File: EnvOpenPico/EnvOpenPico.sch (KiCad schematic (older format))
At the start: 47 parts, among them J2 SKRKAEE020, J3 2.54mm header 01x20, J4 2.54mm header 01x20, J5 Conn_01x03_Male, U1 TPS63002, U3 RP2040, X1 XO 32 12Mhz 3225 seiko

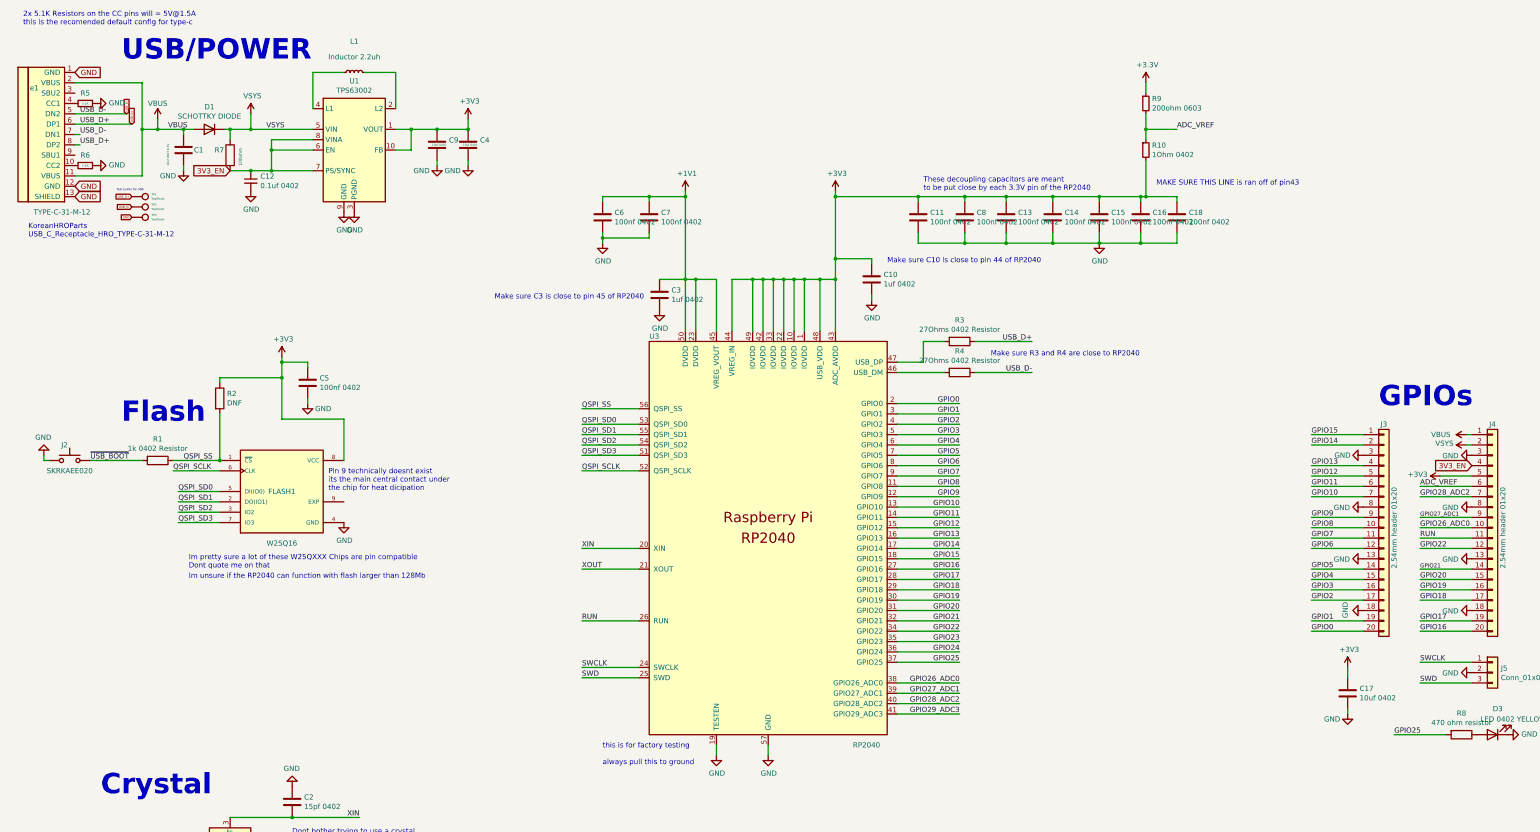
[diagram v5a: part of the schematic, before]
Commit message: added some extra notes and moved some parts about, added some test points.
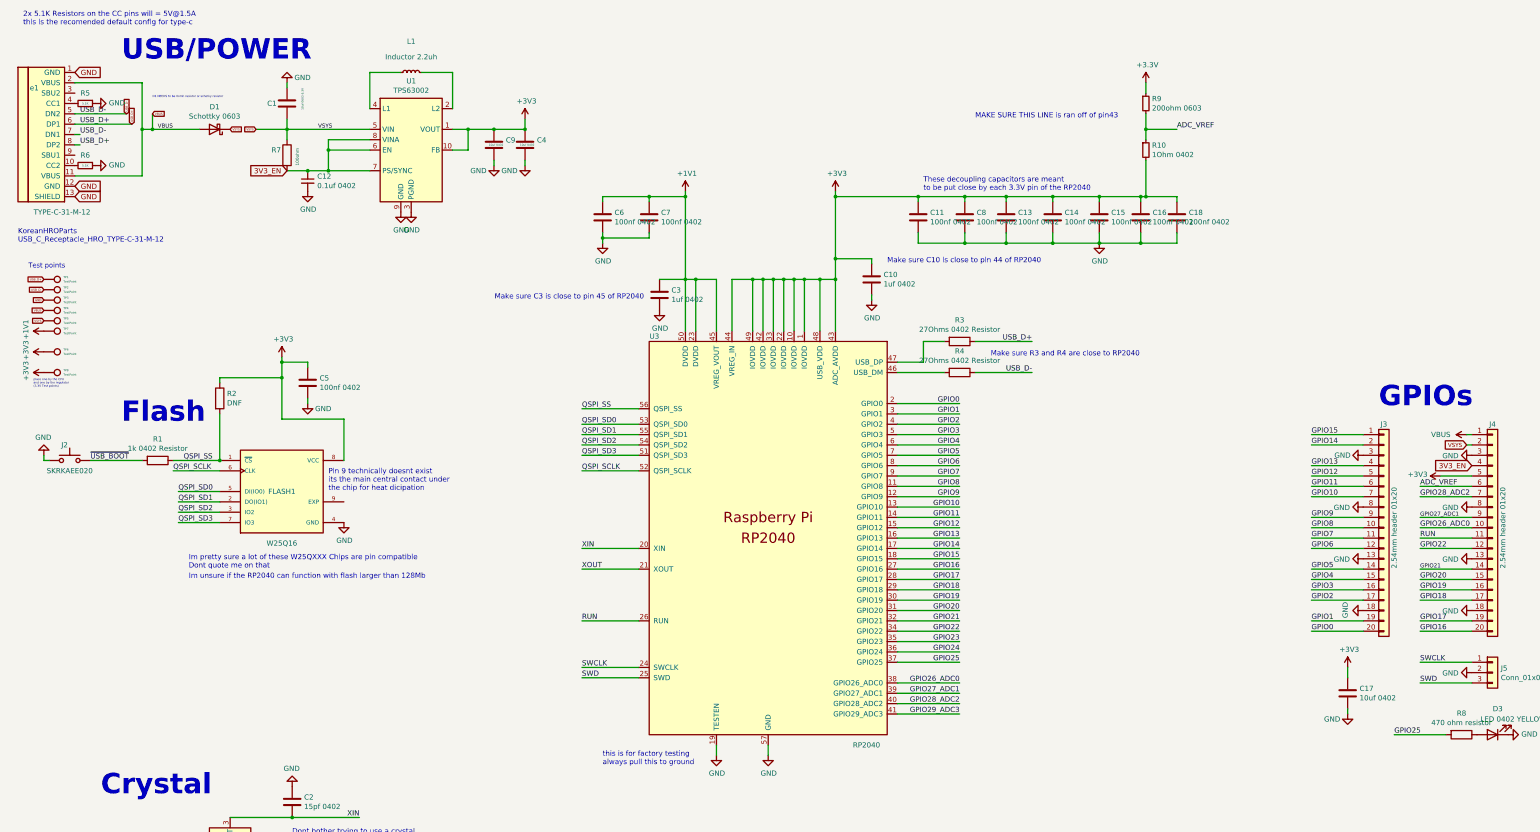
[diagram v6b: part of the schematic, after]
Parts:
- removed D1: SCHOTTKY DIODE, Diode_SMD:D_0603_1608Metric, symbol Simulation_SPICE:DIODE
- added D1: Schottky 0603, Diode_SMD:D_0603_1608Metric, symbol Device:D_Schottky
- added TP4, TP5, TP6, TP7, TP8: TestPoint, TestPoint:TestPoint_Pad_D1.0mm, symbol Connector:TestPoint
- TP1, TP2, TP3: footprint TestPoint:TestPoint_Pad_1.0x1.0mm -> TestPoint:TestPoint_Pad_D1.0mm
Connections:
- net +1V1: now also TP7.1
- net +3V3: now also TP6.1, TP8.1
- net VBUS: now also D1.2 (A), TP4.1; no longer C1.1, J4.2 (Pin_2), R7.1, U1.5 (VIN)
- new net VSYS: C1.1, D1.1 (K), J4.2 (Pin_2), R7.1, TP5.1, U1.5 (VIN)
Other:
- note added: "D1 NEEDS to be 0omh resistor or schotky resistor"
- note added: "Test points"
- note added: "place one by the CPU\nand one by the regulator\n(3.3V Test points)"
- note added: "this is for factory testing\nalways pull this to ground"
- note removed: "Test points for USB"
- note removed: "this is for factory testing\n\nalways pull this to ground"
- moved on the sheet: C1, C12, C4, C9, L1, R7, TP1, TP2, TP3, U1

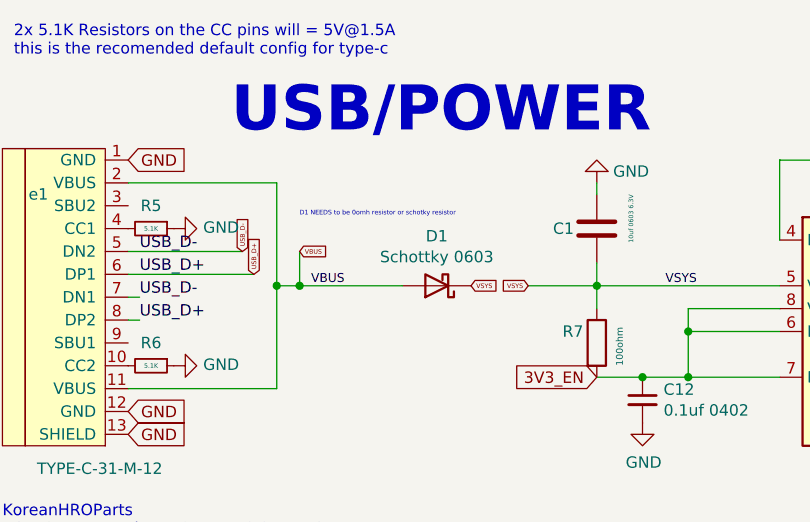
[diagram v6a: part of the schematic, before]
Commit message: changed notes regarding D1 and what type should be installed.
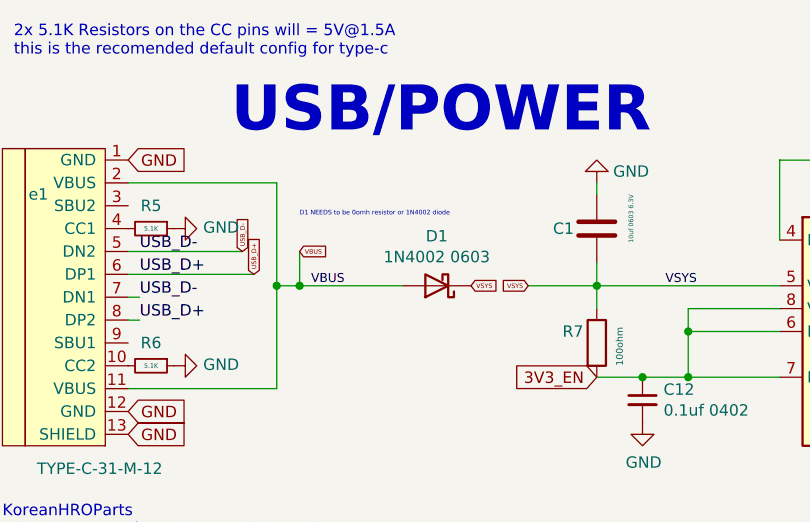
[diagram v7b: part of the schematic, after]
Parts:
- D1: value Schottky 0603 -> 1N4002 0603
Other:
- note added: "D1 NEEDS to be 0omh resistor or 1N4002 diode"
- note removed: "D1 NEEDS to be 0omh resistor or schotky resistor"
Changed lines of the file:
@@
 P 2450 1750
 F 0 "D1" H 2450 1533 50  0000 C CNN
-F 1 "Schottky 0603" H 2450 1624 50  0000 C CNN
+F 1 "1N4002 0603" H 2450 1624 50  0000 C CNN
 F 2 "Diode_SMD:D_0603_1608Metric" H 2450 1750 50  0001 C CNN
 F 3 "~" H 2450 1750 50  0001 C CNN
@@
 $EndComp
 Text Notes 1850 1450 0    20   ~ 0
-D1 NEEDS to be 0omh resistor or schotky resistor
+D1 NEEDS to be 0omh resistor or 1N4002 diode
 Wire Wire Line
 	3950 1200 4250 1200

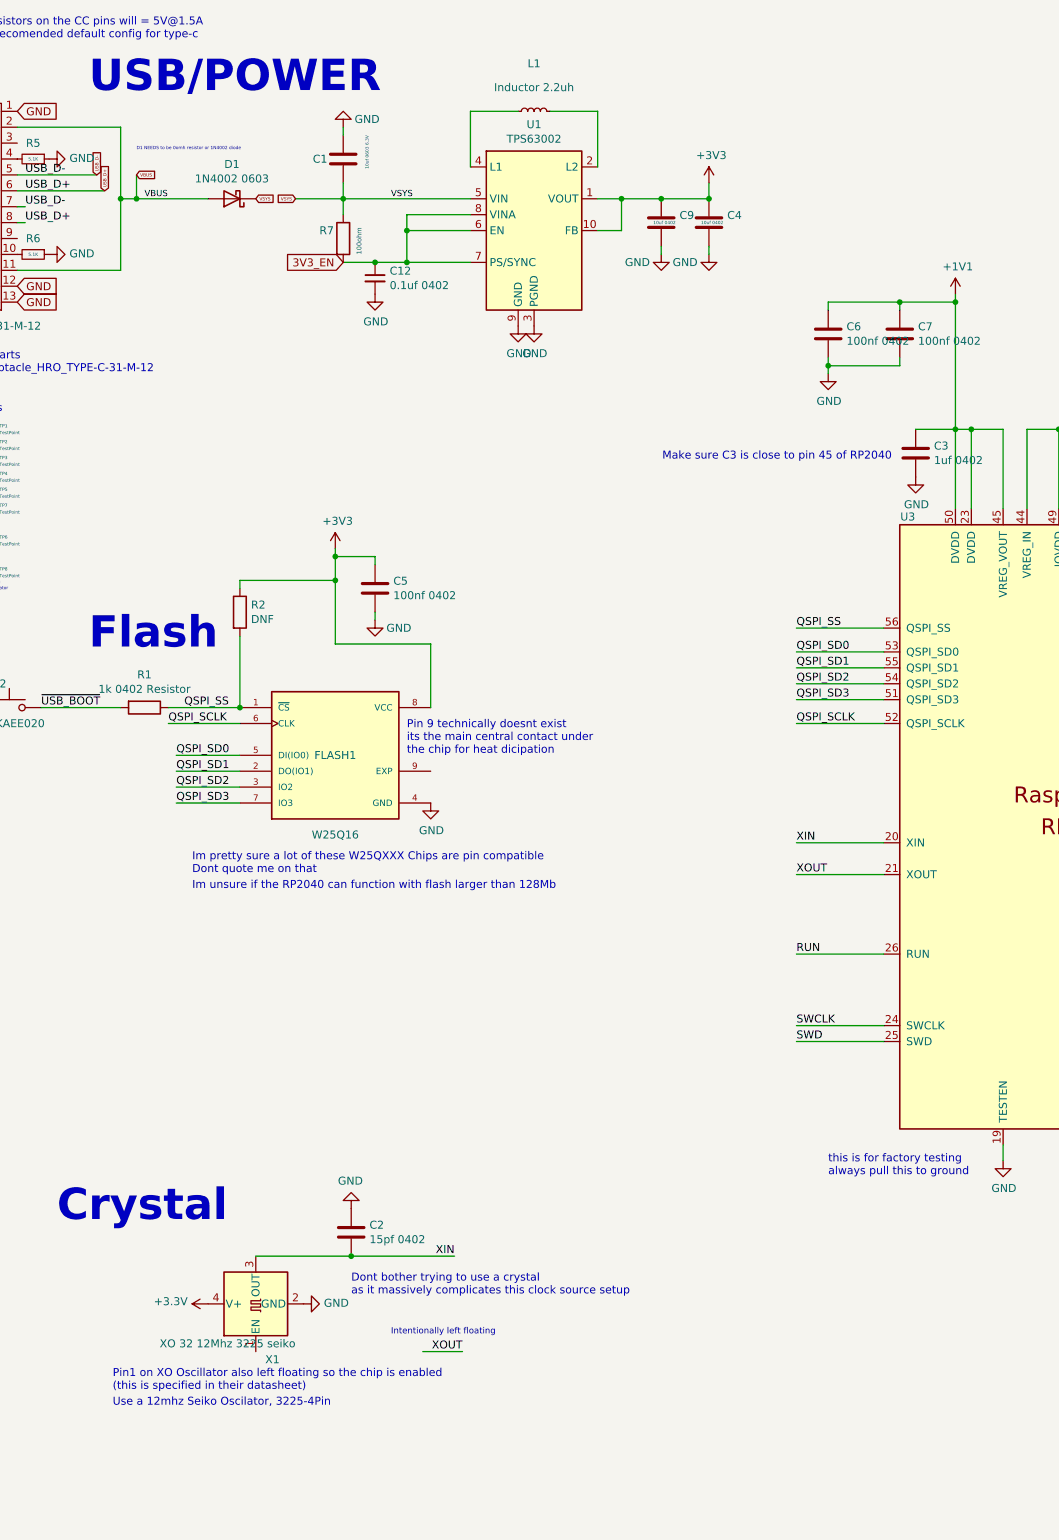
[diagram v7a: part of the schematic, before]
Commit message: replaced XO with crystal due to stock issues, and some general cleanups and corrections
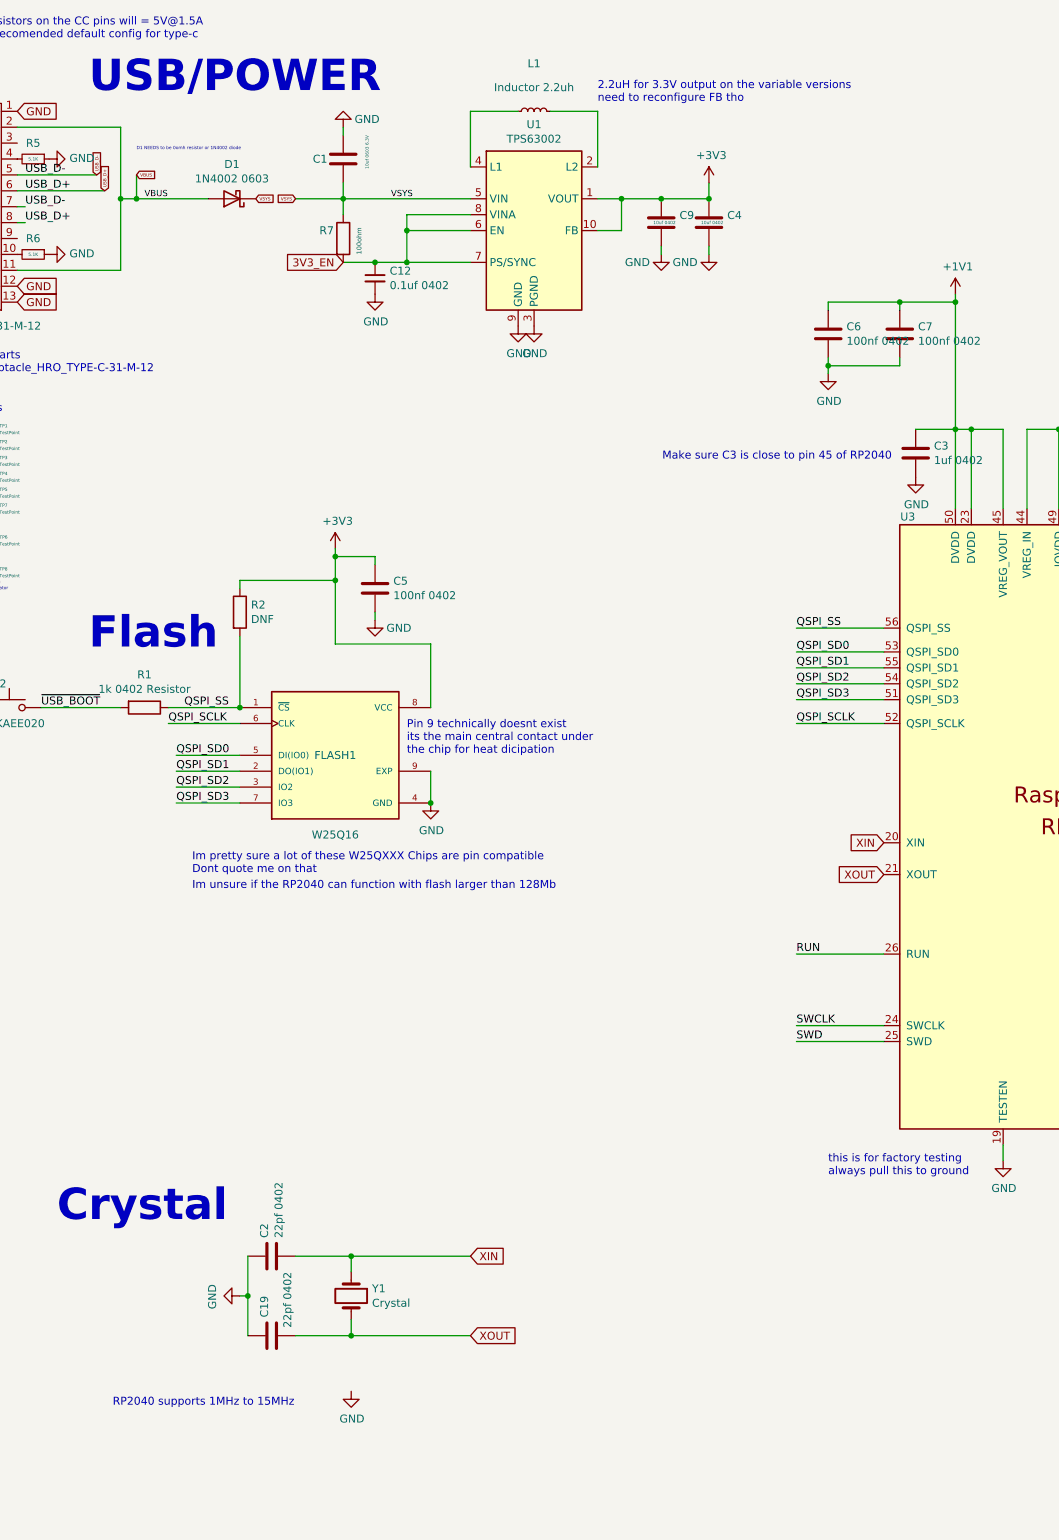
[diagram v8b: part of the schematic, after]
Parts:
- removed X1: XO 32 12Mhz 3225 seiko, Crystal:Crystal_SMD_SeikoEpson_TSX3225-4Pin_3.2x2.5mm, symbol Oscillator:XO32
- added C19: 22pf 0402, Capacitor_SMD:C_0402_1005Metric, symbol Device:C
- added Y1: Crystal, Crystal:Crystal_SMD_5032-2Pin_5.0x3.2mm, symbol Device:Crystal
- C2: value 15pf 0402 -> 22pf 0402
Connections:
- net GND: now also FLASH1.9 (EXP), C19.1
- net XIN: now also Y1.1
- net XOUT: now also C19.2, Y1.2
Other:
- note added: "2.2uH for 3.3V output on the variable versions\nneed to reconfigure FB tho"
- note added: "RP2040 supports 1MHz to 15MHz"
- note removed: "Dont bother trying to use a crystal\nas it massively complicates this clock source setup"
- note removed: "Intentionally left floating"
- note removed: "Pin1 on XO Oscillator also left floating so the chip is enabled\n(this is specified in their datasheet)"
- note removed: "Use a 12mhz Seiko Oscilator, 3225-4Pin"
- moved on the sheet: C2
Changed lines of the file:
@@
 encoding utf-8
 Sheet 1 1
-Title "RP2040 Minimal Design Example"
+Title "Raspberry Pi Pico Clone"
 Date "2020-12-18"
 Rev "REV1"
-Comp "Raspberry Pi (Trading) Ltd"
+Comp "Envious.Design"
 Comment1 ""
 Comment2 ""
@@
 	1    0    0    -1
 $EndComp
-Wire Wire Line
-	6000 5800 6550 5800
-Wire Wire Line
-	6550 6000 6000 6000
 Wire Wire Line
 	6000 4600 6550 4600
@@
 Text Label 6000 4900 0    50   ~ 0
 QSPI_SD3
-Text Label 6000 5800 0    50   ~ 0
-XIN
-Text Label 6000 6000 0    50   ~ 0
-XOUT
 $Comp
 L Device:R R4
@@
 Wire Wire Line
 	13400 6950 13400 7050
-Text Label 3850 8400 2    50   ~ 0
-XIN
-Text Label 3900 9000 2    50   ~ 0
-XOUT
-Wire Wire Line
-	2600 8400 3200 8400
 Text Notes 9950 3950 0    50   ~ 0
 Make sure R3 and R4 are close to RP2040
@@
 	8450 2400 9250 2400
 $Comp
-L Oscillator:XO32 X1
-U 1 1 60894744
-P 2600 8700
-F 0 "X1" V 2250 8550 50  0000 L CNN
-F 1 "XO 32 12Mhz 3225 seiko" V 2350 8450 50  0000 L CNN
-F 2 "Crystal:Crystal_SMD_SeikoEpson_TSX3225-4Pin_3.2x2.5mm" H 3300 8350 50  0001 C CNN
-F 3 "" H 2500 8700 50  0001 C CNN
-	1    2600 8700
-	0    -1   -1   0
-$EndComp
-$Comp
-L power:GND #PWR0105
-U 1 1 608B9527
-P 2900 8700
-F 0 "#PWR0105" H 2900 8450 50  0001 C CNN
-F 1 "GND" V 2905 8572 50  0000 R CNN
-F 2 "" H 2900 8700 50  0001 C CNN
-F 3 "" H 2900 8700 50  0001 C CNN
-	1    2900 8700
-	0    -1   -1   0
-$EndComp
-$Comp
-L power:+3.3V #PWR0106
-U 1 1 608B9D1F
-P 2300 8700
-F 0 "#PWR0106" H 2300 8550 50  0001 C CNN
-F 1 "+3.3V" V 2315 8828 50  0000 L CNN
-F 2 "" H 2300 8700 50  0001 C CNN
-F 3 "" H 2300 8700 50  0001 C CNN
-	1    2300 8700
-	0    -1   -1   0
-$EndComp
-$Comp
 L Device:C C2
 U 1 1 5ED96B87
-P 3200 8250
-F 0 "C2" H 3315 8296 50  0000 L CNN
-F 1 "15pf 0402" H 3315 8205 50  0000 L CNN
-F 2 "Capacitor_SMD:C_0402_1005Metric" H 3238 8100 50  0001 C CNN
-F 3 "" H 3200 8250 50  0001 C CNN
-	1    3200 8250
-	1    0    0    -1
+P 2700 8400
+F 0 "C2" H 2815 8446 50  0000 L CNN
+F 1 "22pf 0402" H 2815 8355 50  0000 L CNN
+F 2 "Capacitor_SMD:C_0402_1005Metric" H 2738 8250 50  0001 C CNN
+F 3 "" H 2700 8400 50  0001 C CNN
+	1    2700 8400
+	0    -1   -1   0
 $EndComp
 Connection ~ 3200 8400
-Wire Wire Line
-	3200 8400 3850 8400
 $Comp
 L power:GND #PWR0107
 U 1 1 6097CBA8
-P 3200 8100
-F 0 "#PWR0107" H 3200 7850 50  0001 C CNN
-F 1 "GND" H 3205 7927 50  0000 C CNN
-F 2 "" H 3200 8100 50  0001 C CNN
-F 3 "" H 3200 8100 50  0001 C CNN
-	1    3200 8100
-	-1   0    0    1
-$EndComp
-Wire Wire Line
-	3650 9000 3900 9000
-Text Notes 3450 8900 0    39   ~ 0
-Intentionally left floating
-Text Notes 1700 9250 0    50   ~ 0
-Pin1 on XO Oscillator also left floating so the chip is enabled\n(this is specified in their datasheet)
+P 2500 8650
+F 0 "#PWR0107" H 2500 8400 50  0001 C CNN
+F 1 "GND" H 2505 8477 50  0000 C CNN
+F 2 "" H 2500 8650 50  0001 C CNN
+F 3 "" H 2500 8650 50  0001 C CNN
+	1    2500 8650
+	0    1    1    0
+$EndComp
 Wire Wire Line
 	7000 2400 7000 3200
@@
 $EndComp
 Text Notes 1700 9350 0    50   ~ 0
-Use a 12mhz Seiko Oscilator, 3225-4Pin
+RP2040 supports 1MHz to 15MHz
 Text Notes 2200 6000 0    50   ~ 0
 Im pretty sure a lot of these W25QXXX Chips are pin compatible\nDont quote me on that
@@
 Text Notes 3550 5250 0    50   ~ 0
 Pin 9 technically doesnt exist\nits the main central contact under\nthe chip for heat dicipation
-Text Notes 3200 8650 0    50   ~ 0
-Dont bother trying to use a crystal\nas it massively complicates this clock source setup
 Text Notes 9300 2350 0    50   ~ 0
 These decoupling capacitors are meant\nto be put close by each 3.3V pin of the RP2040
@@
 place one by the CPU\nand one by the regulator\n(3.3V Test points)
 $Comp
-L power:+1V1 #PWR?
+L power:+1V1 #PWR0115
 U 1 1 610CF35B
 P 800 3700
-F 0 "#PWR?" H 800 3550 50  0001 C CNN
+F 0 "#PWR0115" H 800 3550 50  0001 C CNN
 F 1 "+1V1" H 815 3873 50  0000 C CNN
 F 2 "" H 800 3700 50  0001 C CNN
@@
 	0    -1   -1   0
 $EndComp
+Text Notes 4750 1150 0    50   ~ 0
+2.2uH for 3.3V output on the variable versions\nneed to reconfigure FB tho
+Wire Wire Line
+	3700 5550 3700 5350
+Connection ~ 3700 5550
+$Comp
+L Device:Crystal Y1
+U 1 1 612055A1
+P 3200 8650
+F 0 "Y1" V 3154 8781 50  0000 L CNN
+F 1 "Crystal" V 3245 8781 50  0000 L CNN
+F 2 "Crystal:Crystal_SMD_5032-2Pin_5.0x3.2mm" H 3200 8650 50  0001 C CNN
+F 3 "~" H 3200 8650 50  0001 C CNN
+	1    3200 8650
+	0    1    1    0
+$EndComp
+Wire Wire Line
+	3200 8500 3200 8400
+Wire Wire Line
+	3200 8900 3200 8800
+Wire Wire Line
+	3200 8900 2850 8900
+Connection ~ 3200 8900
+Wire Wire Line
+	2850 8400 3200 8400
+$Comp
+L Device:C C19
+U 1 1 612806FF
+P 2700 8900
+F 0 "C19" H 2815 8946 50  0000 L CNN
+F 1 "22pf 0402" H 2750 8800 50  0000 L CNN
+F 2 "Capacitor_SMD:C_0402_1005Metric" H 2738 8750 50  0001 C CNN
+F 3 "" H 2700 8900 50  0001 C CNN
+	1    2700 8900
+	0    -1   -1   0
+$EndComp
+$Comp
+L power:GND #PWR019
+U 1 1 61280CDE
+P 3200 9250
+F 0 "#PWR019" H 3200 9000 50  0001 C CNN
+F 1 "GND" H 3205 9077 50  0000 C CNN
+F 2 "" H 3200 9250 50  0001 C CNN
+F 3 "" H 3200 9250 50  0001 C CNN
+	1    3200 9250
+	1    0    0    -1
+$EndComp
+Wire Wire Line
+	3200 8400 3950 8400
+Wire Wire Line
+	3200 8900 3950 8900
+Text GLabel 6550 5800 0    50   Input ~ 0
+XIN
+Text GLabel 6550 6000 0    50   Input ~ 0
+XOUT
+Text GLabel 3950 8900 2    50   Input ~ 0
+XOUT
+Text GLabel 3950 8400 2    50   Input ~ 0
+XIN
+Wire Wire Line
+	2550 8900 2550 8650
+Wire Wire Line
+	2550 8650 2500 8650
+Connection ~ 2550 8650
+Wire Wire Line
+	2550 8650 2550 8400
 $EndSCHEMATC
